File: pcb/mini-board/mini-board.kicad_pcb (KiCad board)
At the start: 4 copper layers, 132.1 x 132.1 mm, 56 parts, among them J1 USB_B, J2 EXPANSION BUS, J3 SD Card Board, J4 Atmel-JTAG-10, J5 SYSTEM BUS, J8 SERIAL, SW1 SW_SPDT, SW2 RESET, SW3 NMI, U1 74AC11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

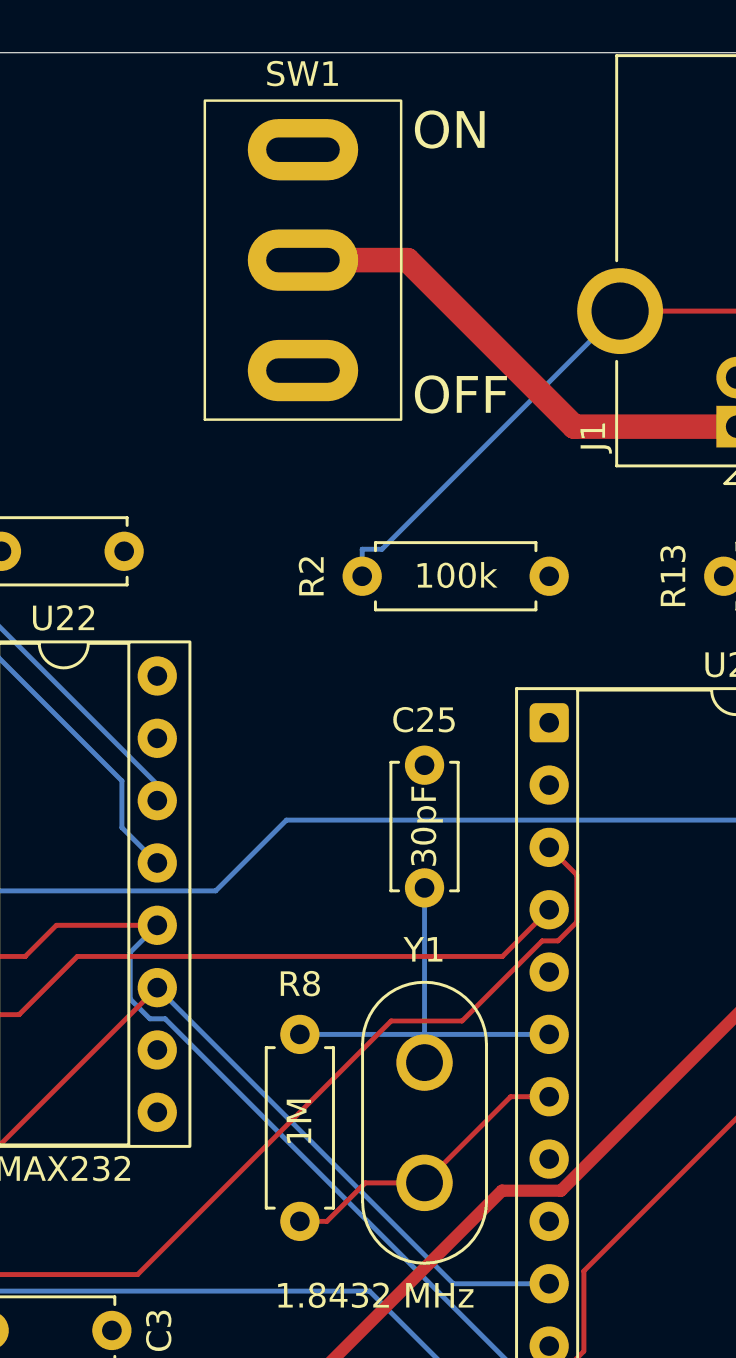
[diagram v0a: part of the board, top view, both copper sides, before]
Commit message: Exposing BCOS ROM and modifying README file
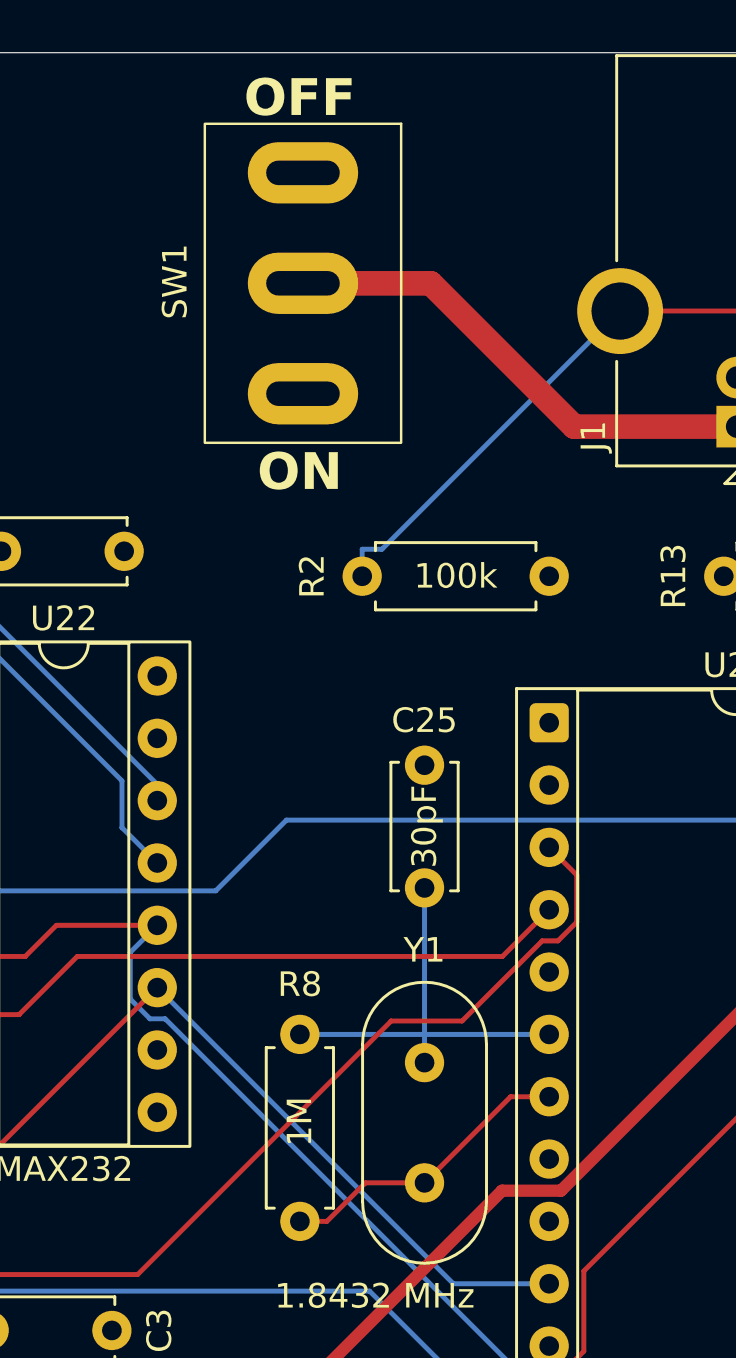
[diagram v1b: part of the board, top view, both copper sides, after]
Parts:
- moved SW1 0.94 mm to (223.6, 34.8), turned to -90 degrees
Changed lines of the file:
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@@
 	(title_block
 		(title "ByteCradle 6502 MINI BOARD")
-		(date "2025-05-03")
-		(rev "rev1")
+		(date "2025-05-11")
+		(rev "rev2")
 	)
 	(layers
 		(0 "F.Cu" signal)
-		(4 "In1.Cu" signal)
-		(6 "In2.Cu" signal)
+		(4 "In1.Cu" power)
+		(6 "In2.Cu" power)
 		(2 "B.Cu" signal)
 		(9 "F.Adhes" user "F.Adhesive")
@@
 	(footprint "components:power_switch"
 		(layer "F.Cu")
-		(at 223.647 33.854 90)
+		(at 223.647 34.798 -90)
 		(property "Reference" "SW1"
-			(at 7.565 0 0)
+			(at -0.072 5.207 90)
 			(unlocked yes)
 			(layer "F.SilkS")
@@
 		)
 		(property "Value" "SW_SPDT"
-			(at 0 -6.5 90)
+			(at 0 -6.5 270)
 			(unlocked yes)
 			(layer "F.Fab")
@@
 		)
 		(property "Datasheet" ""
-			(at 0 0 90)
+			(at 0 0 270)
 			(unlocked yes)
 			(layer "F.Fab")
@@
 		)
 		(property "Description" "Switch, single pole double throw"
-			(at 0 0 90)
+			(at 0 0 270)
 			(unlocked yes)
 			(layer "F.Fab")
@@
 		)
 		(fp_text user "${REFERENCE}"
-			(at 0 5.5 90)
+			(at 0 5.5 270)
 			(unlocked yes)
 			(layer "F.Fab")
@@
 		)
 		(pad "1" thru_hole oval
-			(at -4.5 0 90)
+			(at -4.5 0 270)
 			(size 2.5 4.5)
 			(drill oval 1 3)
@@
 		)
 		(pad "2" thru_hole oval
-			(at 0 0 90)
+			(at 0 0 270)
 			(size 2.5 4.5)
 			(drill oval 1 3)
@@
 		)
 		(pad "3" thru_hole oval
-			(at 4.5 0 90)
+			(at 4.5 0 270)
 			(size 2.5 4.5)
 			(drill oval 1 3)
@@
 		(at 239.776 149.86)
 		(property "Reference" "G001"
-			(at 0 0 0)
+			(at 0 9.144 0)
 			(layer "Dwgs.User")
 			(effects
@@
 		(pad "1" thru_hole circle
 			(at 0 0 90)
-			(size 2.3 2.3)
-			(drill 1.5)
+			(size 1.6 1.6)
+			(drill 0.8)
 			(layers "*.Cu" "*.Mask")
 			(remove_unused_layers no)
@@
 		(pad "2" thru_hole circle
 			(at 4.9 0 90)
-			(size 2.3 2.3)
-			(drill 1.5)
+			(size 1.6 1.6)
+			(drill 0.8)
 			(layers "*.Cu" "*.Mask")
 			(remove_unused_layers no)
@@
 	)
 	(gr_text "OFF"
-		(at 228.092 40.259 0)
+		(at 223.52 28.122 0)
 		(layer "F.SilkS" knockout)
 		(effects
 			(font
 				(size 1.5 1.5)
-				(thickness 0.2)
+				(thickness 0.3)
+				(bold yes)
 			)
-			(justify left bottom)
+			(justify bottom)
 		)
 	)
@@
 	)
 	(gr_text "ON"
-		(at 228.092 29.464 0)
+		(at 223.52 43.362 0)
 		(layer "F.SilkS" knockout)
 		(effects
 			(font
 				(size 1.5 1.5)
-				(thickness 0.2)
+				(thickness 0.3)
+				(bold yes)
 			)
-			(justify left bottom)
+			(justify bottom)
 		)
 	)
@@
 	)
 	(segment
-		(start 234.696 40.64)
-		(end 227.91 33.854)
+		(start 228.854 34.798)
+		(end 223.647 34.798)
 		(width 1)
 		(layer "F.Cu")
@@
 	)
 	(segment
-		(start 227.91 33.854)
-		(end 223.647 33.854)
+		(start 234.696 40.64)
+		(end 228.854 34.798)
 		(width 1)
 		(layer "F.Cu")
